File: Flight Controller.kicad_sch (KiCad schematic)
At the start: 133 parts, among them IC1 ICM-20689, IC2 AT7456E, J1 Micro_SD_Card, J2 USB_C_Receptacle_USB2.0_14P, Q1 BC817W, U1 STM32F405RGTx, U2 LMR51430, U3 BMP280, U4 NCP1117-3.3_SOT223, U5 LMR51430

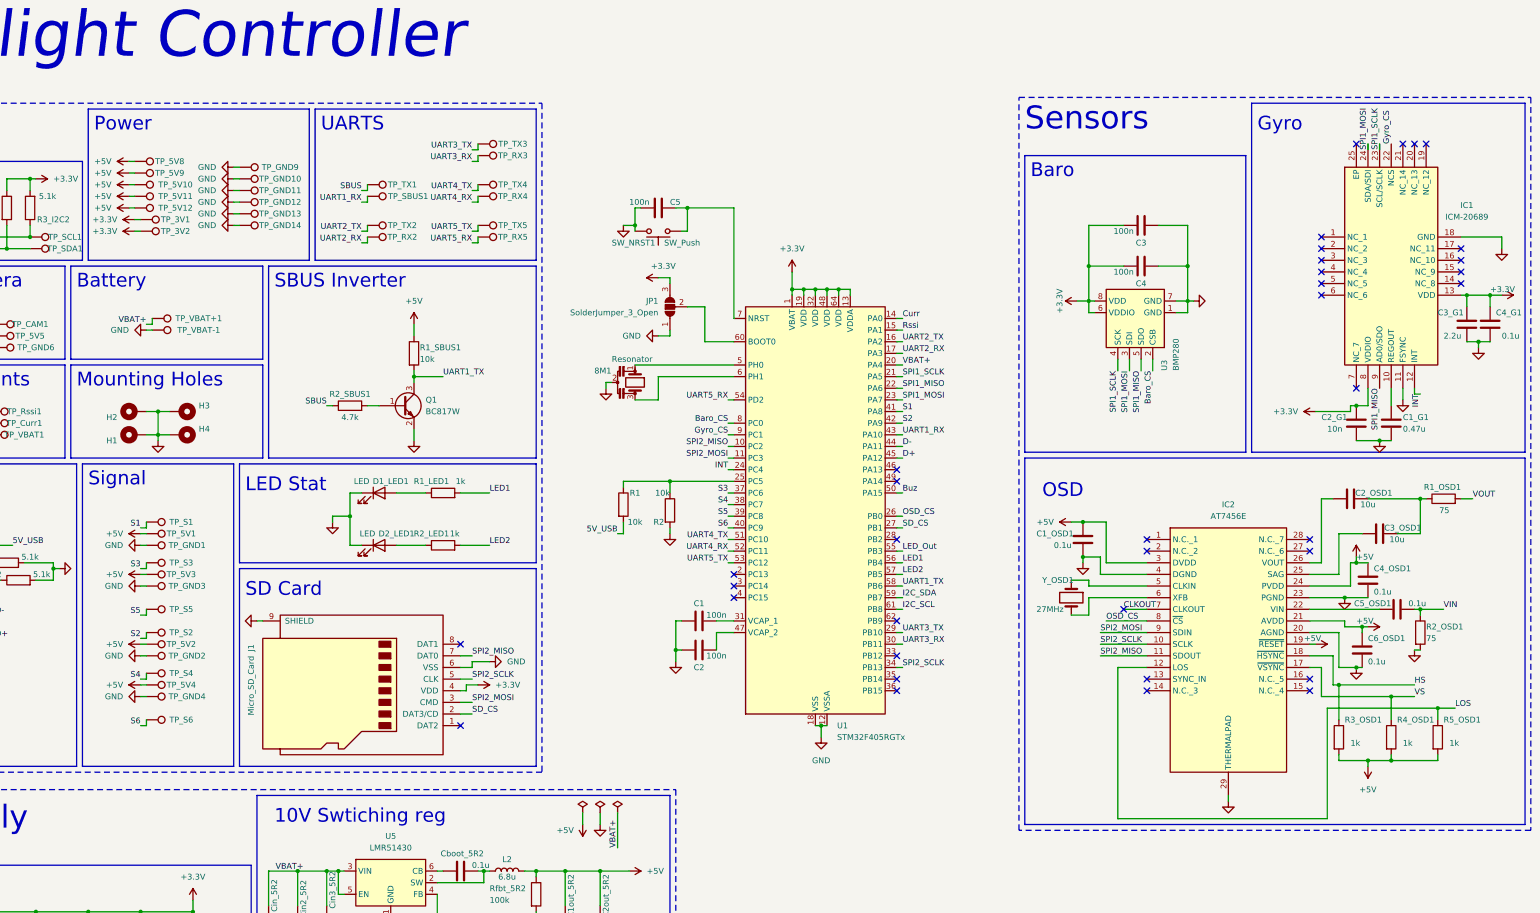
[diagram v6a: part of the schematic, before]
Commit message: Changes to compline with Betaflighe guidlines
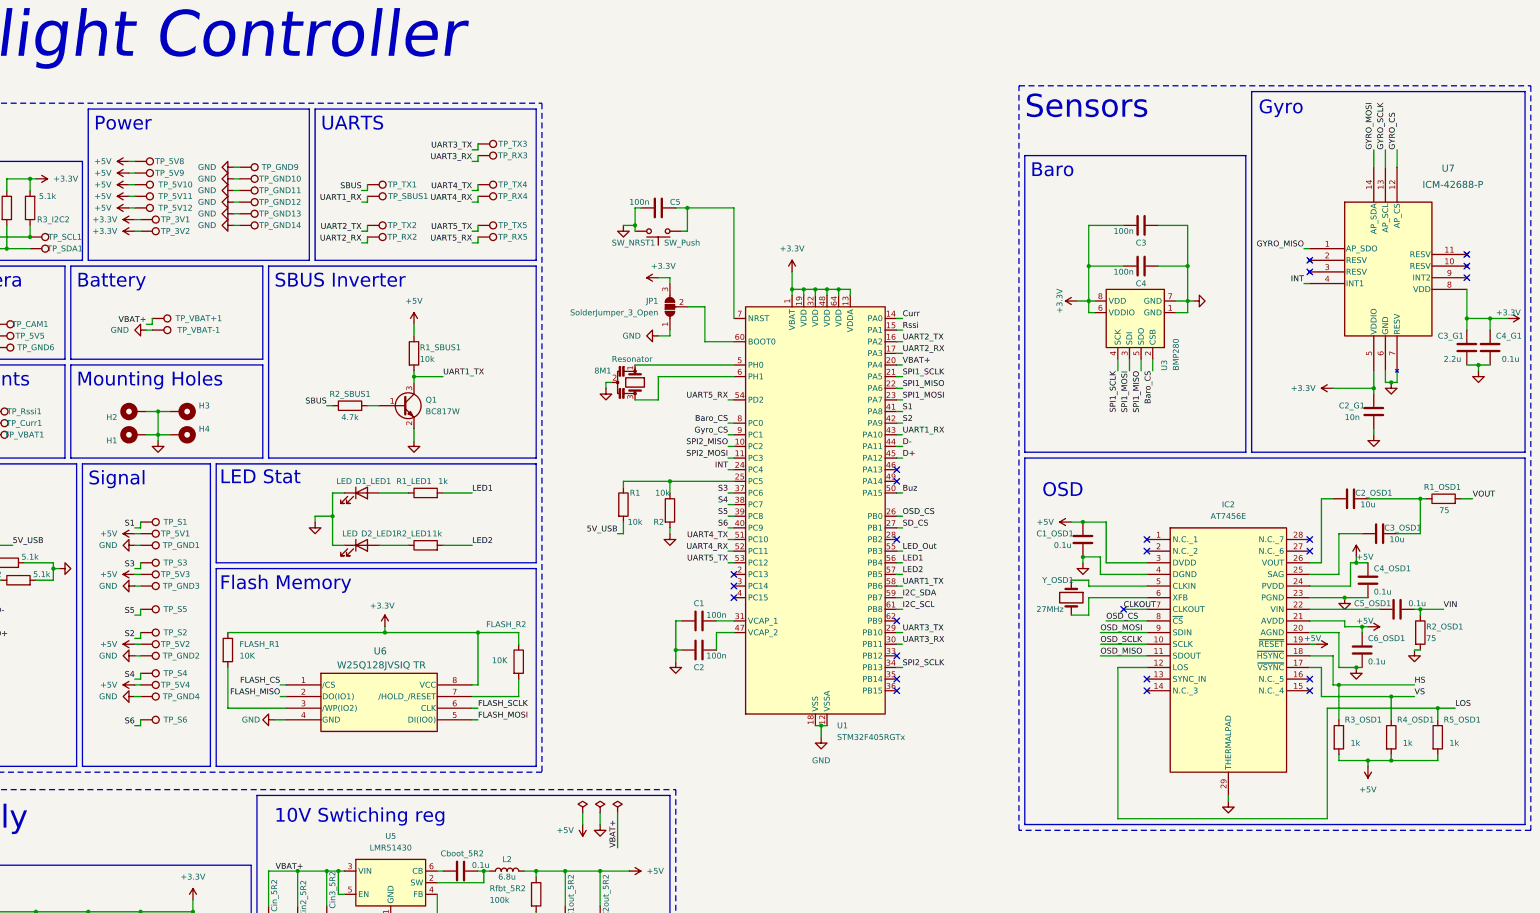
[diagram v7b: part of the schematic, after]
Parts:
- removed C1_G1: 0.47u, Capacitor_SMD:C_0402_1005Metric, symbol Device:C
- removed IC1: ICM-20689, ICM-20689:QFN50P400X400X95-24N, symbol ICM-20689:ICM-20689
- removed J1: Micro_SD_Card, Connector_Card:microSD_HC_Molex_47219-2001, symbol Connector:Micro_SD_Card
- added FLASH_R1, FLASH_R2: 10K, symbol Device:R
- added U6: W25Q128JVSIQ TR, SOIC_208MIL_WIN, symbol W25Q128FV:W25Q128JVSIQ_TR
- added U7: ICM-42688-P, LGA14_2P5X3X0P91_TDK, symbol ICM-42688-P:ICM-42688-P
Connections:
- net +3.3V: now also FLASH_R1.1, FLASH_R2.1, U6.8 (VCC), U7.5 (VDDIO), U7.8 (VDD)
- net GND: now also U6.4 (GND), U7.6 (GND), U7.7 (RESV)
- net INT: now also U7.4 (INT1)
- net SPI2_MISO: no longer IC2.11 (SDOUT)
- net SPI2_MOSI: no longer IC2.9 (SDIN)
- net SPI2_SCLK: no longer IC2.10 (SCLK)
- new net: FLASH_R1.2, U6.3 (/WP(IO2))
- new net: FLASH_R2.2, U6.7 (/HOLD_/RESET)
- new net FLASH_CS: U6.1 (/CS)
- new net FLASH_MISO: U6.2 (DO(IO1))
- new net FLASH_MOSI: U6.5 (DI(IO0))
- new net FLASH_SCLK: U6.6 (CLK)
- new net GYRO_CS: U7.12 (AP_CS)
- new net GYRO_MISO: U7.1 (AP_SDO)
- new net GYRO_MOSI: U7.14 (AP_SDA)
- new net GYRO_SCLK: U7.13 (AP_SCL)
- new net OSD_MISO: IC2.11 (SDOUT)
- new net OSD_MOSI: IC2.9 (SDIN)
- new net OSD_SCLK: IC2.10 (SCLK)
- no-connect marks 36 -> 24
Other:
- note added: "Flash Memory"
- note removed: "SD Card"
- moved on the sheet: C2_G1, C3_G1, C4_G1, D1_LED1, D2_LED1, R1_LED1, R2_LED1, TP_5V1, TP_5V2, TP_5V3, TP_5V4, TP_GND1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

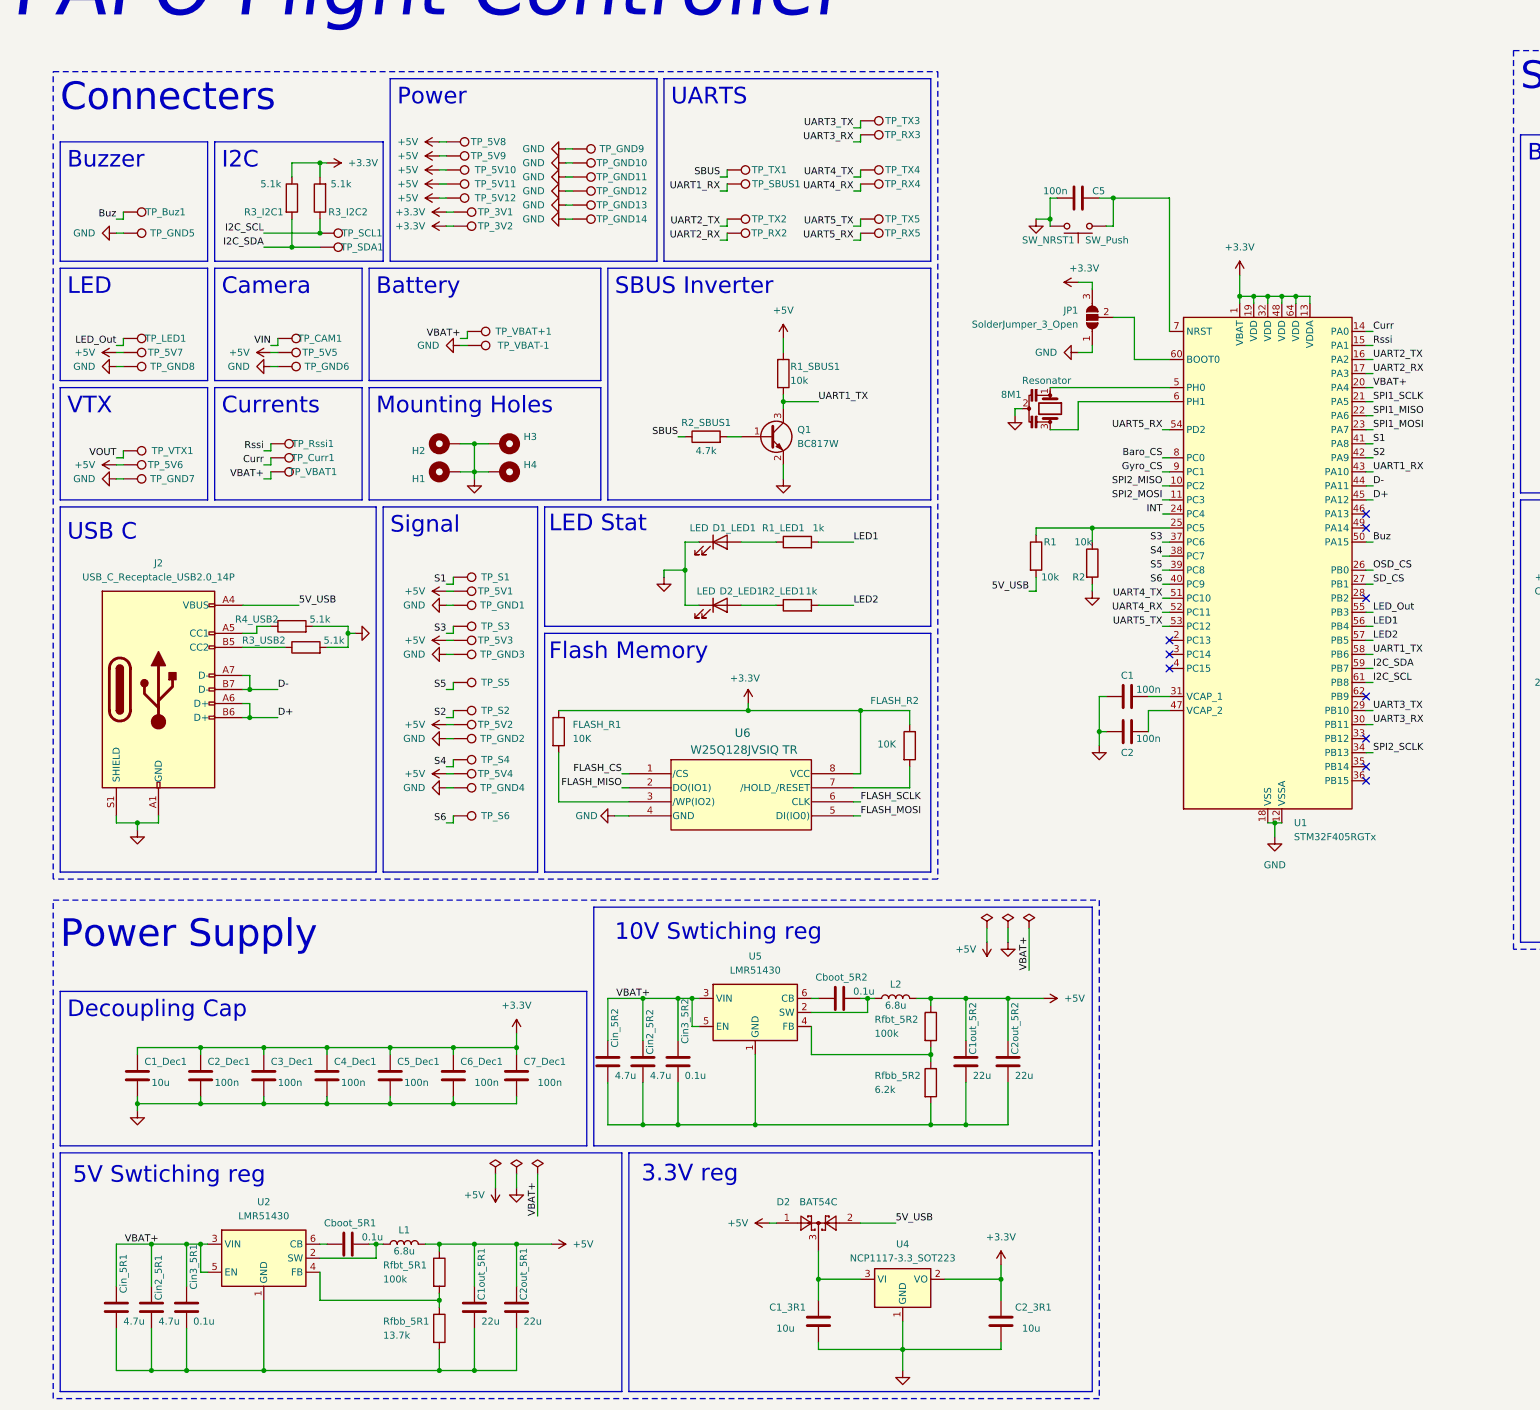
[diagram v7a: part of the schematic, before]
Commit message: assgining new pins
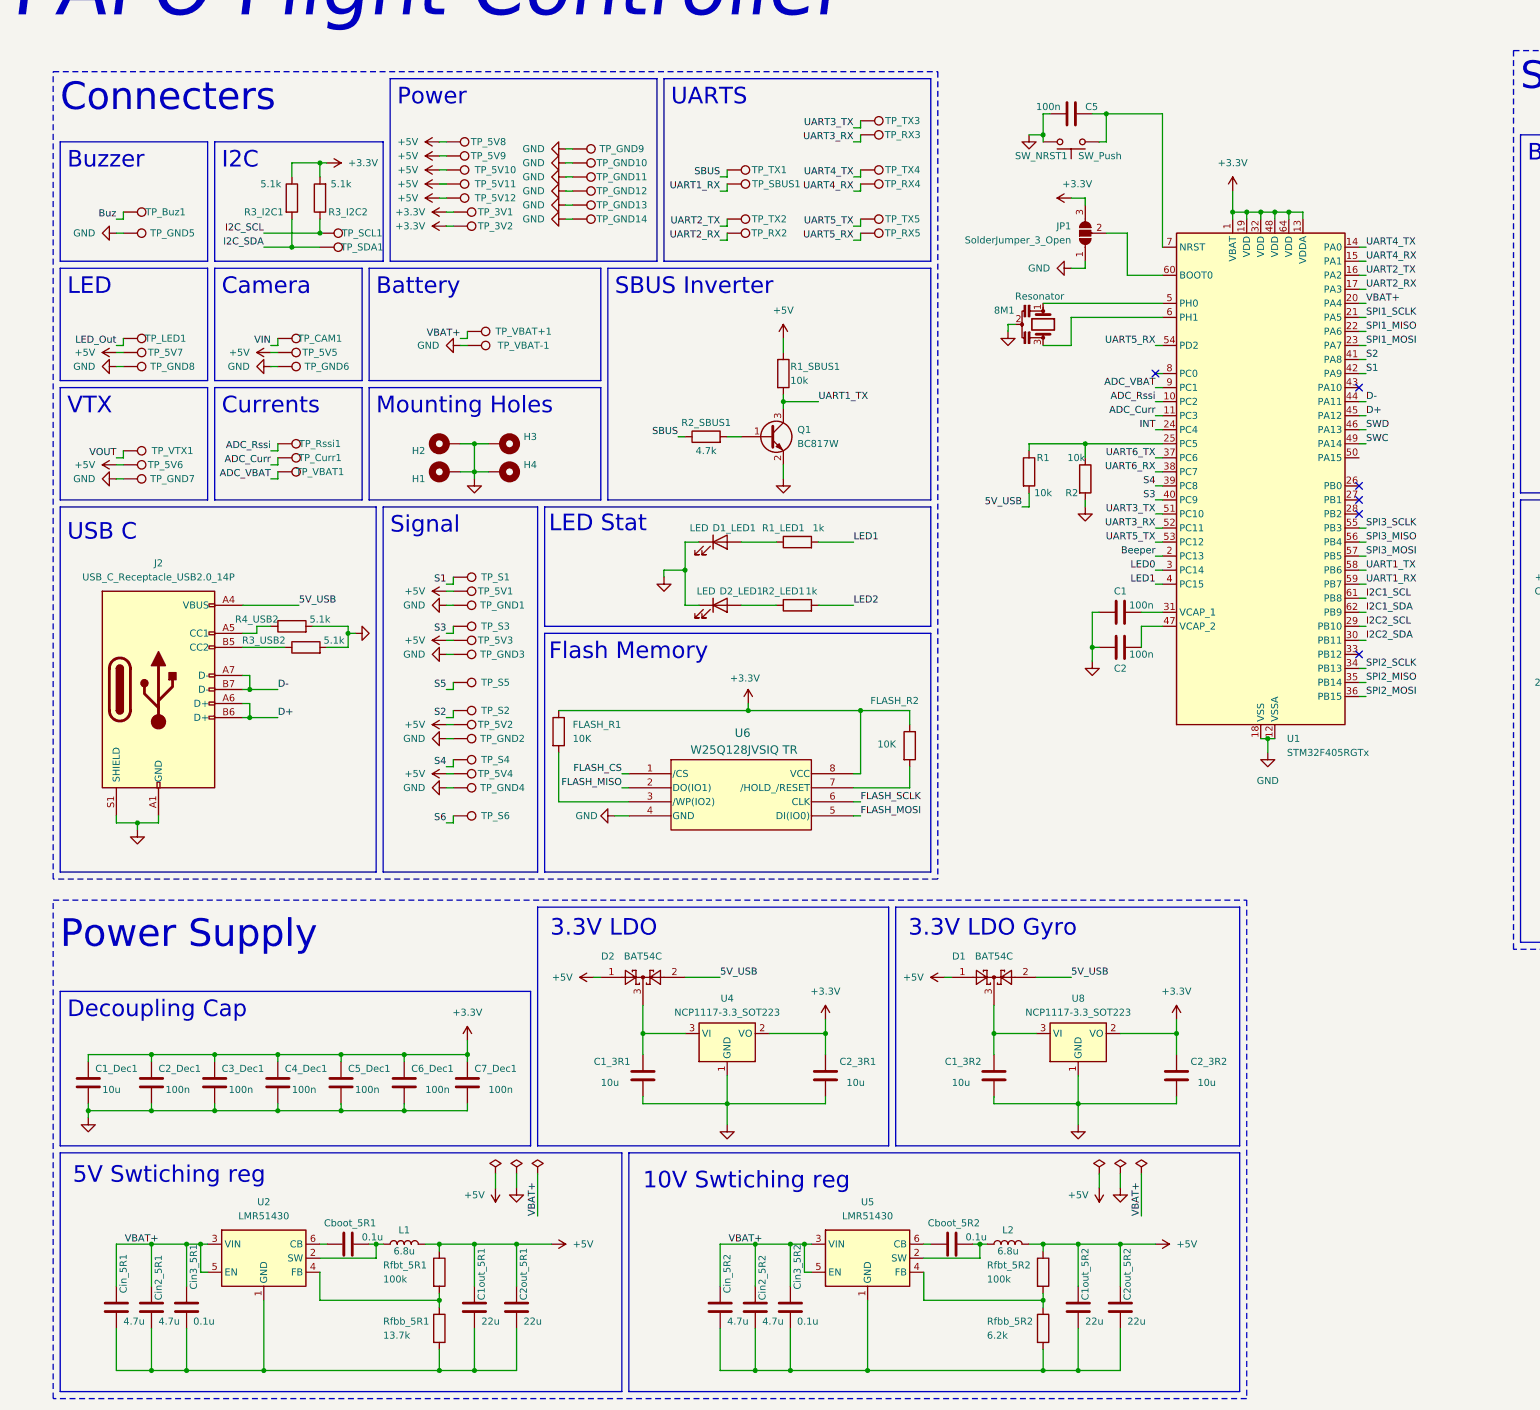
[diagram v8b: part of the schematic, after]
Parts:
- added C1_3R2, C2_3R2: 10u, Capacitor_SMD:C_0805_2012Metric, symbol Device:C
- added D1: BAT54C, Package_TO_SOT_SMD:SOT-23, symbol Diode:BAT54C
- added U8: NCP1117-3.3_SOT223, Package_TO_SOT_SMD:SOT-223-3_TabPin2, symbol Regulator_Linear:NCP1117-3.3_SOT223
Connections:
- net +3.3V: now also C2_3R2.1, U8.2 (VO)
- net +5V: now also D1.1
- net 5V_USB: now also D1.2
- net Baro_CS: no longer U1.8 (PC0)
- net Buz: no longer U1.50 (PA15)
- net GND: now also C1_3R2.2, C2_3R2.2, U8.1 (GND)
- net I2C_SCL: no longer U1.61 (PB8)
- net I2C_SDA: no longer U1.59 (PB7)
- net LED1: now also U1.4 (PC15); no longer U1.56 (PB4)
- net LED2: no longer U1.57 (PB5)
- net LED_Out: no longer U1.55 (PB3)
- net OSD_CS: no longer U1.26 (PB0)
- net S1: now also U1.42 (PA9); no longer U1.41 (PA8)
- net S2: now also U1.41 (PA8); no longer U1.42 (PA9)
- net S3: now also U1.40 (PC9); no longer U1.37 (PC6)
- net S4: now also U1.39 (PC8); no longer U1.38 (PC7)
- net S5: no longer U1.39 (PC8)
- net S6: no longer U1.40 (PC9)
- net SPI2_MISO: now also U1.35 (PB14); no longer U1.10 (PC2)
- net SPI2_MOSI: now also U1.36 (PB15); no longer U1.11 (PC3)
- net UART1_RX: now also U1.59 (PB7); no longer U1.43 (PA10)
- net UART3_RX: now also U1.52 (PC11); no longer U1.30 (PB11)
- net UART3_TX: now also U1.51 (PC10); no longer U1.29 (PB10)
- net UART4_RX: now also U1.15 (PA1); no longer U1.52 (PC11)
- net UART4_TX: now also U1.14 (PA0); no longer U1.51 (PC10)
- net VBAT+: no longer TP_VBAT1.1
- net Beeper: now reaches U1.2 (PC13)
- net LED0: now reaches U1.3 (PC14)
- net SWD: now reaches U1.46 (PA13)
- net SWC: now reaches U1.49 (PA14)
- net I2C1_SDA: now reaches U1.62 (PB9)
- net Curr renamed ADC_Curr
- net ADC_Curr: now also U1.11 (PC3); no longer U1.14 (PA0)
- net Gyro_CS renamed ADC_VBAT
- net ADC_VBAT: now also TP_VBAT1.1
- net Rssi renamed ADC_Rssi
- net ADC_Rssi: now also U1.10 (PC2); no longer U1.15 (PA1)
- net SD_CS: no longer names the net of U1.27 (PB1)
- new net: C1_3R2.1, D1.3, U8.3 (VI)
- new net I2C1_SCL: U1.61 (PB8)
- new net I2C2_SCL: U1.29 (PB10)
- new net I2C2_SDA: U1.30 (PB11)
- new net SPI3_MISO: U1.56 (PB4)
- new net SPI3_MOSI: U1.57 (PB5)
- new net SPI3_SCLK: U1.55 (PB3)
- new net UART6_RX: U1.38 (PC7)
- new net UART6_TX: U1.37 (PC6)
- no-connect marks 24 -> 20
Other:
- note added: "3.3V LDO"
- note added: "3.3V LDO Gyro"
- note removed: "3.3V reg"
- moved on the sheet: 8M1, C1, C1_3R1, C1_Dec1, C1out_5R2, C2, C2_3R1, C2_Dec1, C2out_5R2, C3_Dec1, C4_Dec1, C5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
